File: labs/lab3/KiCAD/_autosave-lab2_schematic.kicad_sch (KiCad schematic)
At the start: 17 parts, among them M1 Fan, SW1 Push Button, SW2 RotaryEncoder, U2 ATmega328P µC

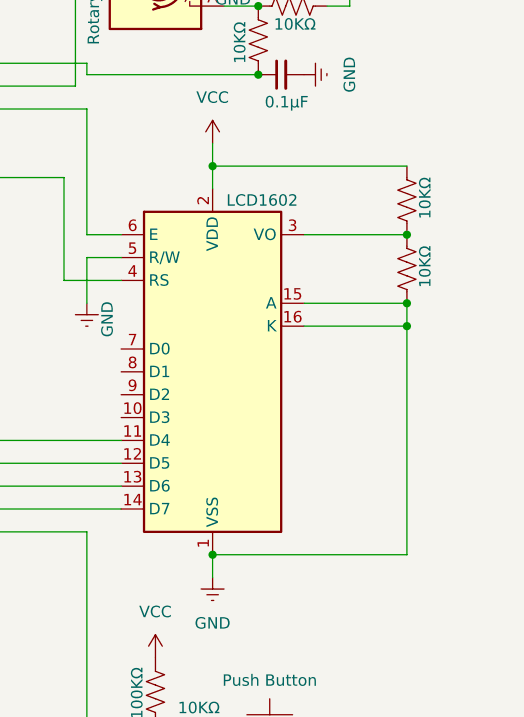
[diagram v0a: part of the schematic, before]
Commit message: lab 4 report intro and conclusion. No enery to write discussion section
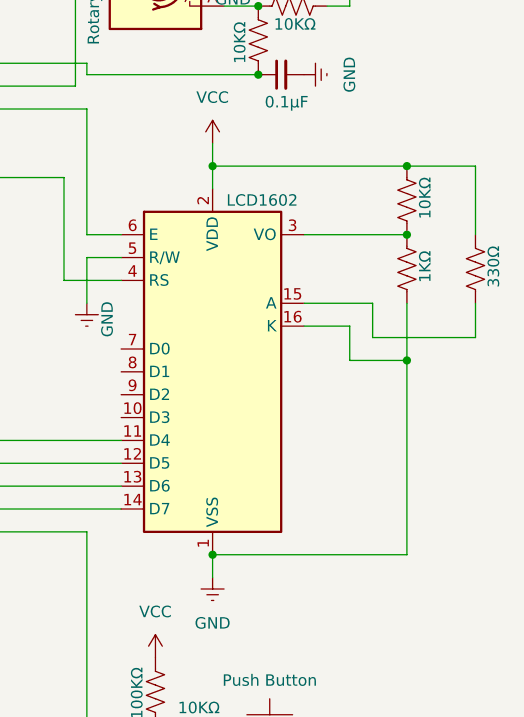
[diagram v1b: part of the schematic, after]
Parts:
- added R9: 330Ω, symbol Device:R_US
- R8: value 10KΩ -> 1KΩ
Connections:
- net GND: no longer LCD1602.15 (A)
- net VCC: now also R9.2
- new net: LCD1602.15 (A), R9.1
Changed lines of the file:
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@@
-	)
-	(junction
-		(at 143.51 92.71)
-		(diameter 0)
-		(color 0 0 0 0)
 	)
 	(junction
@@
 	)
 	(junction
+		(at 143.51 99.06)
+		(diameter 0)
+		(color 0 0 0 0)
+	)
+	(junction
 		(at 127 46.99)
 		(diameter 0)
@@
 	)
 	(junction
-		(at 143.51 95.25)
+		(at 143.51 85.09)
 		(diameter 0)
 		(color 0 0 0 0)
 	)
 	(junction
-		(at 143.51 85.09)
+		(at 143.51 77.47)
 		(diameter 0)
 		(color 0 0 0 0)
@@
 	(wire
 		(pts
+			(xy 151.13 85.09) (xy 151.13 77.47)
+		)
+		(stroke
+			(width 0)
+			(type default)
+		)
+	)
+	(wire
+		(pts
 			(xy 95.25 139.7) (xy 104.14 139.7)
 		)
@@
 	(wire
 		(pts
+			(xy 143.51 77.47) (xy 151.13 77.47)
+		)
+		(stroke
+			(width 0)
+			(type default)
+		)
+	)
+	(wire
+		(pts
 			(xy 107.95 87.63) (xy 107.95 92.71)
 		)
@@
 	(wire
 		(pts
+			(xy 137.16 95.25) (xy 137.16 99.06)
+		)
+		(stroke
+			(width 0)
+			(type default)
+		)
+	)
+	(wire
+		(pts
 			(xy 93.98 91.44) (xy 93.98 110.49)
 		)
@@
 	(wire
 		(pts
-			(xy 143.51 95.25) (xy 143.51 92.71)
-		)
-		(stroke
-			(width 0)
-			(type default)
-		)
-	)
-	(wire
-		(pts
 			(xy 115.57 139.7) (xy 107.95 139.7)
 		)
@@
 	(wire
 		(pts
+			(xy 139.7 92.71) (xy 139.7 96.52)
+		)
+		(stroke
+			(width 0)
+			(type default)
+		)
+	)
+	(wire
+		(pts
 			(xy 121.92 120.65) (xy 143.51 120.65)
 		)
@@
 	(wire
 		(pts
-			(xy 132.08 95.25) (xy 143.51 95.25)
+			(xy 137.16 99.06) (xy 143.51 99.06)
+		)
+		(stroke
+			(width 0)
+			(type default)
+		)
+	)
+	(wire
+		(pts
+			(xy 132.08 92.71) (xy 139.7 92.71)
 		)
 		(stroke
@@
 	(wire
 		(pts
+			(xy 132.08 95.25) (xy 137.16 95.25)
+		)
+		(stroke
+			(width 0)
+			(type default)
+		)
+	)
+	(wire
+		(pts
 			(xy 83.82 148.59) (xy 87.63 148.59)
 		)
@@
 	(wire
 		(pts
-			(xy 132.08 92.71) (xy 143.51 92.71)
+			(xy 151.13 92.71) (xy 151.13 96.52)
 		)
 		(stroke
@@
 	(wire
 		(pts
+			(xy 139.7 96.52) (xy 151.13 96.52)
+		)
+		(stroke
+			(width 0)
+			(type default)
+		)
+	)
+	(wire
+		(pts
+			(xy 143.51 99.06) (xy 143.51 120.65)
+		)
+		(stroke
+			(width 0)
+			(type default)
+		)
+	)
+	(wire
+		(pts
 			(xy 63.5 55.88) (xy 63.5 58.42)
 		)
@@
 	(wire
 		(pts
-			(xy 143.51 120.65) (xy 143.51 95.25)
+			(xy 143.51 92.71) (xy 143.51 99.06)
 		)
 		(stroke
@@
 			)
 		)
-		(property "Value" "10KΩ"
+		(property "Value" "1KΩ"
 			(at 145.542 88.646 90)
 			(effects
@@
 					(unit 1)
 				)
+			)
+		)
+	)
+	(symbol
+		(lib_id "Device:R_US")
+		(at 151.13 88.9 180)
+		(unit 1)
+		(exclude_from_sim no)
+		(in_bom yes)
+		(on_board yes)
+		(dnp no)
+		(property "Reference" "R9"
+			(at 157.48 88.9 90)
+			(effects
+				(font
+					(size 1.27 1.27)
+				)
+				(hide yes)
+			)
+		)
+		(property "Value" "330Ω"
+			(at 153.162 88.646 90)
+			(effects
+				(font
+					(size 1.27 1.27)
+				)
+			)
+		)
+		(property "Footprint" ""
+			(at 150.114 88.646 90)
+			(effects
+				(font
+					(size 1.27 1.27)
+				)
+				(hide yes)
+			)
+		)
+		(property "Datasheet" "~"
+			(at 151.13 88.9 0)
+			(effects
+				(font
+					(size 1.27 1.27)
+				)
+				(hide yes)
+			)
+		)
+		(property "Description" "Resistor, US symbol"
+			(at 151.13 88.9 0)
+			(effects
+				(font
+					(size 1.27 1.27)
+				)
+				(hide yes)
+			)
+		)
+		(pin "2"
+		)
+		(pin "1"
+		)
+		(instances
+			(project "lab2_schematic"
+				(path "/5a9f816b-81f3-4b3b-b305-817caf4bd656"
+					(reference "R9")
+					(unit 1)
+				)
